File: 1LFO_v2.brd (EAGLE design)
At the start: 95.6 x 17.8 mm, 23 parts, among them IC1 LM324D

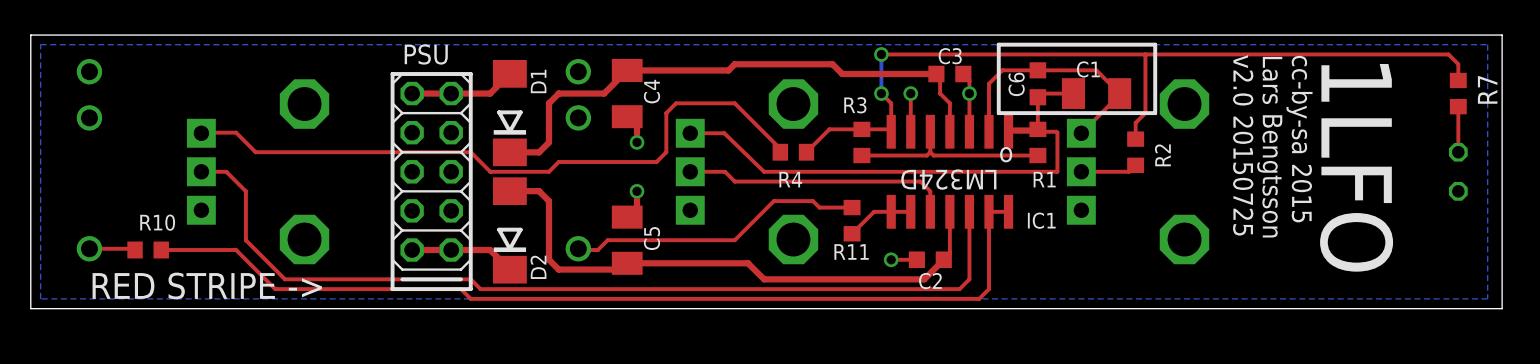
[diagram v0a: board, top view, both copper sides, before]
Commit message: Added switch to select LFO rate range. Moved IC1 & rerouted to make room for the same.
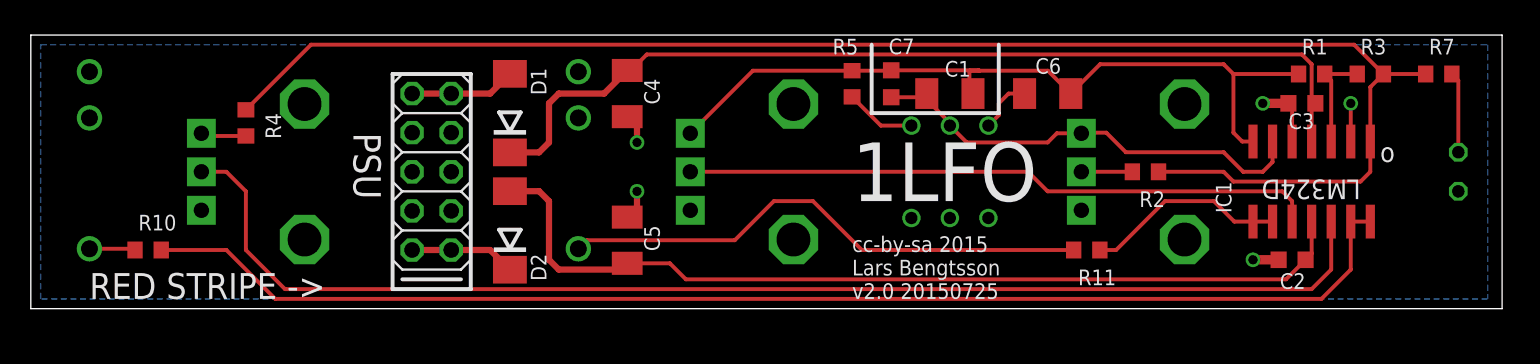
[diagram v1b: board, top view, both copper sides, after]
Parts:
- added C7: 1u, rcl:C0603K
- added R5: 220k, rcl:R0603
- added SW1: TL2285, lb_devs:TL2285_PCB
- C1: value 10u -> 1u
- C6: device rcl:C0603K -> rcl:C1206K
- moved R4 35.6 mm to (17.8, 13.3), turned to 270 degrees
- moved R3 33.3 mm to (90.8, 16.5), turned to 180 degrees
- moved IC1 23.5 mm to (87.0, 9.53)
- moved C2 23.5 mm to (85.7, 4.45)
- moved C3 22.9 mm to (86.4, 14.6), turned to 180 degrees
- moved R1 18.3 mm to (87.0, 16.5), turned to 180 degrees
- moved R11 15.4 mm to (72.4, 5.08), turned to 0 degrees
- moved C1 9.53 mm to (63.5, 15.2), turned to 0 degrees
- moved R7 1.80 mm to (95.2, 16.5), turned to 0 degrees
- moved R2 1.42 mm to (76.2, 10.2), turned to 180 degrees
- moved C6 0.90 mm to (69.8, 15.2), turned to 0 degrees
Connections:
- new net N$4: C6.1, SW1.4
- new net N$6: R5.1, SW1.6
- net GND: now also IC1.2, IC1.5; no longer IC1.3, IC1.6
- net N$1: now also C7.1, IC1.6, SW1.5; no longer C6.1, IC1.2
- net N$5: now also IC1.3; no longer IC1.5
- net SQR: now also IC1.1; no longer IC1.7
- net TRI: now also C7.2, IC1.7, R5.2; no longer IC1.1
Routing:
- net SQR: track 56.0 -> 100.4 mm, vias 2 -> 0
- net N$3: track 43.4 -> 2.96 mm
- net +12V: track 35.9 -> 61.7 mm
- net N$9: track 17.4 -> 41.2 mm
- net N$2: track 59.5 -> 82.4 mm
- net -12V: track 36.9 -> 59.8 mm
- net N$14: track 61.6 -> 83.7 mm
- net N$17: track 19.3 -> 34.8 mm
- net TRI: track 37.1 -> 50.5 mm
- net N$1: track 16.2 -> 29.4 mm
- net N$8: track 4.40 -> 13.1 mm
- net N$5: track 12.9 -> 6.67 mm
- net N$6: track 0.00 -> 4.62 mm
- net N$4: track 0.00 -> 3.66 mm
- net N$13: track 2.96 -> 5.25 mm

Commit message: Minor routing polish :)
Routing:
- net N$4: track 3.66 -> 4.28 mm
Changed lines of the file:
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@@
 </class>
 </classes>
-<designrules name="LaenPCBOrder">
+<designrules name="LaenPCBOrder *">
 <description language="de">&lt;b&gt;EAGLE Design Rules&lt;/b&gt;
 &lt;p&gt;
@@
 <param name="srMinRoundness" value="0mil"/>
 <param name="srMaxRoundness" value="0mil"/>
-<param name="slThermalIsolate" value="10mil"/>
+<param name="slThermalIsolate" value="12mil"/>
 <param name="slThermalsForVias" value="0"/>
 <param name="dpMaxLengthDifference" value="10mm"/>
@@
 </element>
 <element name="IC1" library="linear" package="SO14" value="LM324D" x="86.995" y="9.525" smashed="yes" rot="R180">
-<attribute name="NAME" x="80.772" y="9.525" size="1.016" layer="25" font="vector" rot="R270"/>
+<attribute name="NAME" x="91.567" y="10.16" size="1.016" layer="25" font="vector" rot="R270"/>
 <attribute name="VALUE" x="90.17" y="9.652" size="1.27" layer="25" font="vector" rot="SR180"/>
 </element>
@@
 <wire x1="84.455" y1="10.795" x2="83.82" y2="10.16" width="0.254" layer="1"/>
 <wire x1="83.82" y1="10.16" x2="82.55" y2="10.16" width="0.254" layer="1"/>
-<wire x1="82.55" y1="10.16" x2="81.28" y2="11.43" width="0.254" layer="1"/>
-<wire x1="81.28" y1="11.43" x2="74.93" y2="11.43" width="0.254" layer="1"/>
-<wire x1="74.93" y1="11.43" x2="73.66" y2="12.7" width="0.254" layer="1"/>
+<wire x1="82.55" y1="10.16" x2="80.645" y2="12.065" width="0.254" layer="1"/>
+<wire x1="80.645" y1="12.065" x2="74.295" y2="12.065" width="0.254" layer="1"/>
+<wire x1="74.295" y1="12.065" x2="73.66" y2="12.7" width="0.254" layer="1"/>
 <wire x1="73.66" y1="12.7" x2="72.08" y2="12.7" width="0.254" layer="1"/>
 <wire x1="72.08" y1="12.7" x2="72.04" y2="12.66" width="0.254" layer="1"/>
@@
 <wire x1="89.75" y1="18.415" x2="22.01" y2="18.415" width="0.254" layer="1"/>
 <wire x1="22.01" y1="18.415" x2="17.78" y2="14.185" width="0.254" layer="1"/>
-<wire x1="77.05" y1="10.16" x2="81.28" y2="10.16" width="0.254" layer="1"/>
-<wire x1="81.28" y1="10.16" x2="81.915" y2="9.525" width="0.254" layer="1"/>
-<wire x1="81.915" y1="9.525" x2="90.17" y2="9.525" width="0.254" layer="1"/>
+<wire x1="77.05" y1="10.16" x2="80.01" y2="10.16" width="0.254" layer="1"/>
+<wire x1="80.01" y1="10.16" x2="80.645" y2="9.525" width="0.254" layer="1"/>
+<wire x1="80.645" y1="9.525" x2="90.17" y2="9.525" width="0.254" layer="1"/>
 <wire x1="90.17" y1="9.525" x2="90.805" y2="10.16" width="0.254" layer="1"/>
 <wire x1="90.805" y1="10.16" x2="90.805" y2="12.125" width="0.254" layer="1"/>
@@
 <wire x1="86.995" y1="12.125" x2="86.995" y2="14.365" width="0.254" layer="1"/>
 <wire x1="86.995" y1="14.365" x2="87.235" y2="14.605" width="0.254" layer="1"/>
-<wire x1="42.545" y1="16.74" x2="42.775" y2="16.74" width="0.254" layer="1"/>
-<wire x1="42.775" y1="16.74" x2="43.815" y2="17.78" width="0.254" layer="1"/>
-<wire x1="43.815" y1="17.78" x2="86.36" y2="17.78" width="0.254" layer="1"/>
+<wire x1="50.165" y1="17.78" x2="86.36" y2="17.78" width="0.254" layer="1"/>
 <wire x1="86.36" y1="17.78" x2="86.995" y2="17.145" width="0.254" layer="1"/>
 <wire x1="86.995" y1="17.145" x2="86.995" y2="14.845" width="0.254" layer="1"/>
 <wire x1="86.995" y1="14.845" x2="87.235" y2="14.605" width="0.254" layer="1"/>
+<wire x1="42.545" y1="16.74" x2="49.125" y2="16.74" width="0.254" layer="1"/>
+<wire x1="49.125" y1="16.74" x2="50.165" y2="17.78" width="0.254" layer="1"/>
 </signal>
 <signal name="-12V">
@@
 <wire x1="38.1" y1="3.81" x2="42.14" y2="3.81" width="0.4064" layer="1"/>
 <wire x1="42.14" y1="3.81" x2="42.545" y2="4.215" width="0.4064" layer="1"/>
-<wire x1="42.545" y1="4.215" x2="45.315" y2="4.215" width="0.254" layer="1"/>
-<wire x1="45.315" y1="4.215" x2="46.355" y2="3.175" width="0.254" layer="1"/>
-<wire x1="46.355" y1="3.175" x2="85.33" y2="3.175" width="0.254" layer="1"/>
+<wire x1="42.545" y1="4.215" x2="49.125" y2="4.215" width="0.254" layer="1"/>
+<wire x1="49.125" y1="4.215" x2="50.165" y2="3.175" width="0.254" layer="1"/>
+<wire x1="50.165" y1="3.175" x2="85.33" y2="3.175" width="0.254" layer="1"/>
 <wire x1="86.995" y1="6.925" x2="86.995" y2="4.84" width="0.254" layer="1"/>
 <wire x1="86.995" y1="4.84" x2="86.6" y2="4.445" width="0.254" layer="1"/>
@@
 <contactref element="R11" pad="2"/>
 <wire x1="84.455" y1="6.925" x2="83.185" y2="6.925" width="0.254" layer="1"/>
-<wire x1="83.185" y1="6.925" x2="81.975" y2="6.925" width="0.254" layer="1"/>
-<wire x1="81.975" y1="6.925" x2="80.645" y2="8.255" width="0.254" layer="1"/>
-<wire x1="80.645" y1="8.255" x2="77.47" y2="8.255" width="0.254" layer="1"/>
+<wire x1="83.185" y1="6.925" x2="81.34" y2="6.925" width="0.254" layer="1"/>
+<wire x1="81.34" y1="6.925" x2="80.01" y2="8.255" width="0.254" layer="1"/>
+<wire x1="80.01" y1="8.255" x2="77.47" y2="8.255" width="0.254" layer="1"/>
 <wire x1="77.47" y1="8.255" x2="74.295" y2="5.08" width="0.254" layer="1"/>
 <wire x1="74.295" y1="5.08" x2="73.24" y2="5.08" width="0.254" layer="1"/>
@@
 <contactref element="IC1" pad="10"/>
 <contactref element="TRI.AM." pad="P$2"/>
-<wire x1="46.64" y1="10.16" x2="68.58" y2="10.16" width="0.254" layer="1"/>
-<wire x1="68.58" y1="10.16" x2="69.85" y2="8.89" width="0.254" layer="1"/>
-<wire x1="69.85" y1="8.89" x2="85.09" y2="8.89" width="0.254" layer="1"/>
+<wire x1="46.64" y1="10.16" x2="69.215" y2="10.16" width="0.254" layer="1"/>
+<wire x1="69.215" y1="10.16" x2="70.485" y2="8.89" width="0.254" layer="1"/>
+<wire x1="70.485" y1="8.89" x2="85.09" y2="8.89" width="0.254" layer="1"/>
 <wire x1="85.09" y1="8.89" x2="85.725" y2="8.255" width="0.254" layer="1"/>
 <wire x1="85.725" y1="8.255" x2="85.725" y2="6.925" width="0.254" layer="1"/>
@@
 <contactref element="SW1" pad="4"/>
 <contactref element="C6" pad="1"/>
-<wire x1="68.35" y1="15.24" x2="67.31" y2="15.24" width="0.254" layer="1"/>
-<wire x1="67.31" y1="15.24" x2="66.675" y2="14.605" width="0.254" layer="1"/>
-<wire x1="66.675" y1="14.605" x2="66.675" y2="13.835" width="0.254" layer="1"/>
-<wire x1="66.675" y1="13.835" x2="66" y2="13.16" width="0.254" layer="1"/>
+<wire x1="66" y1="13.16" x2="67.77" y2="13.16" width="0.254" layer="1"/>
+<wire x1="67.77" y1="13.16" x2="68.58" y2="13.97" width="0.254" layer="1"/>
+<wire x1="68.58" y1="13.97" x2="68.58" y2="15.01" width="0.254" layer="1"/>
+<wire x1="68.58" y1="15.01" x2="68.35" y2="15.24" width="0.254" layer="1"/>
 </signal>
 <signal name="N$6">
